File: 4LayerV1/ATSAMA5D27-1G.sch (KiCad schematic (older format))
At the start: 172 parts, among them J1 Conn_01x16, J2 Conn_01x12, J3 USB_B_Micro, J4 Conn_01x02, J5 Conn_01x02, J6 1051620001, J7 USB_A_Micro, Q1 BSS138, Q2 BSS138, Q3 BSS138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

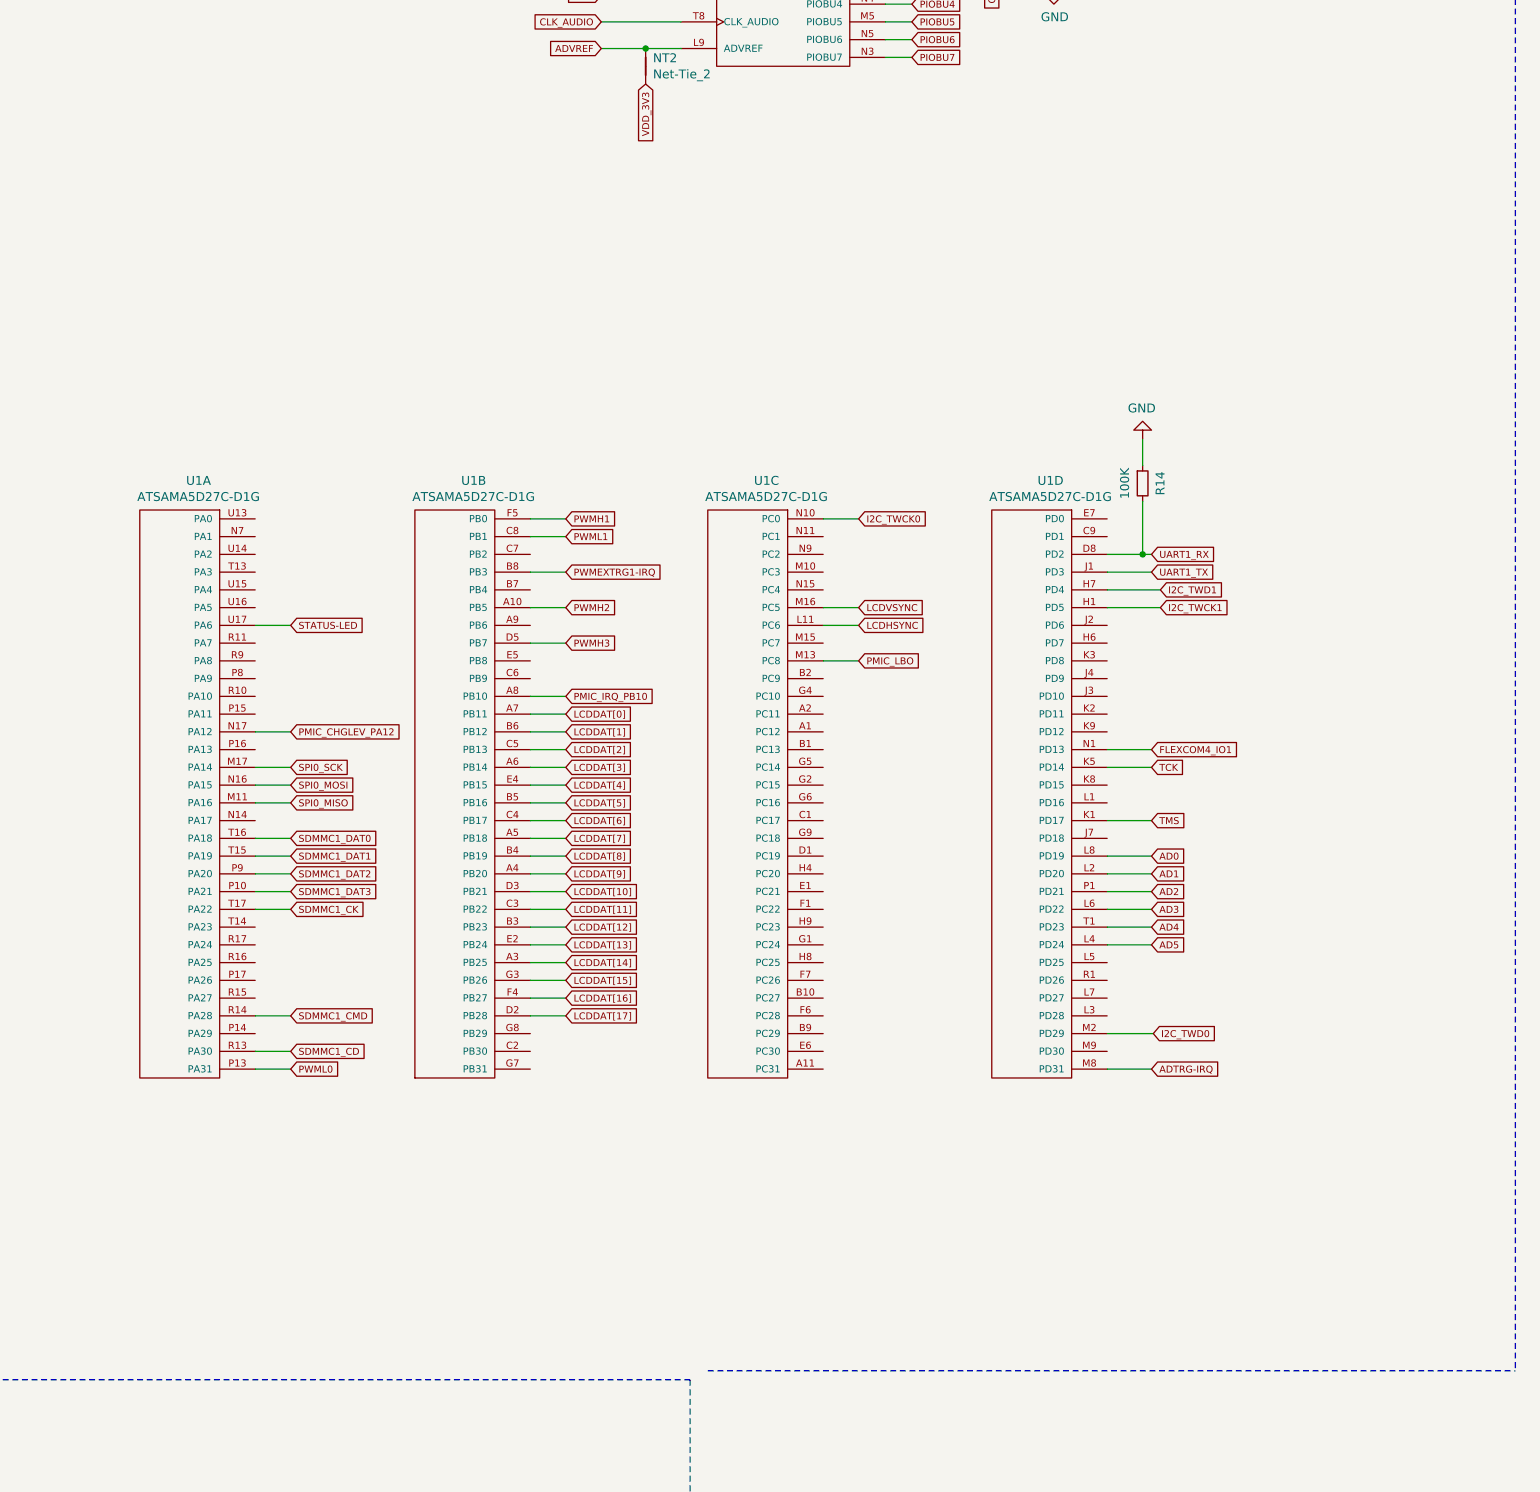
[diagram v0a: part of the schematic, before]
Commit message: Complete 3x 6-bit R2R DACs, with THS7316 buffer.
Using a generic 6-pin connector, as the DE15HD is never going to fit
on the Feather Form factor. I'm not even sure we can get a 6 pin 1mm
pitch header in.
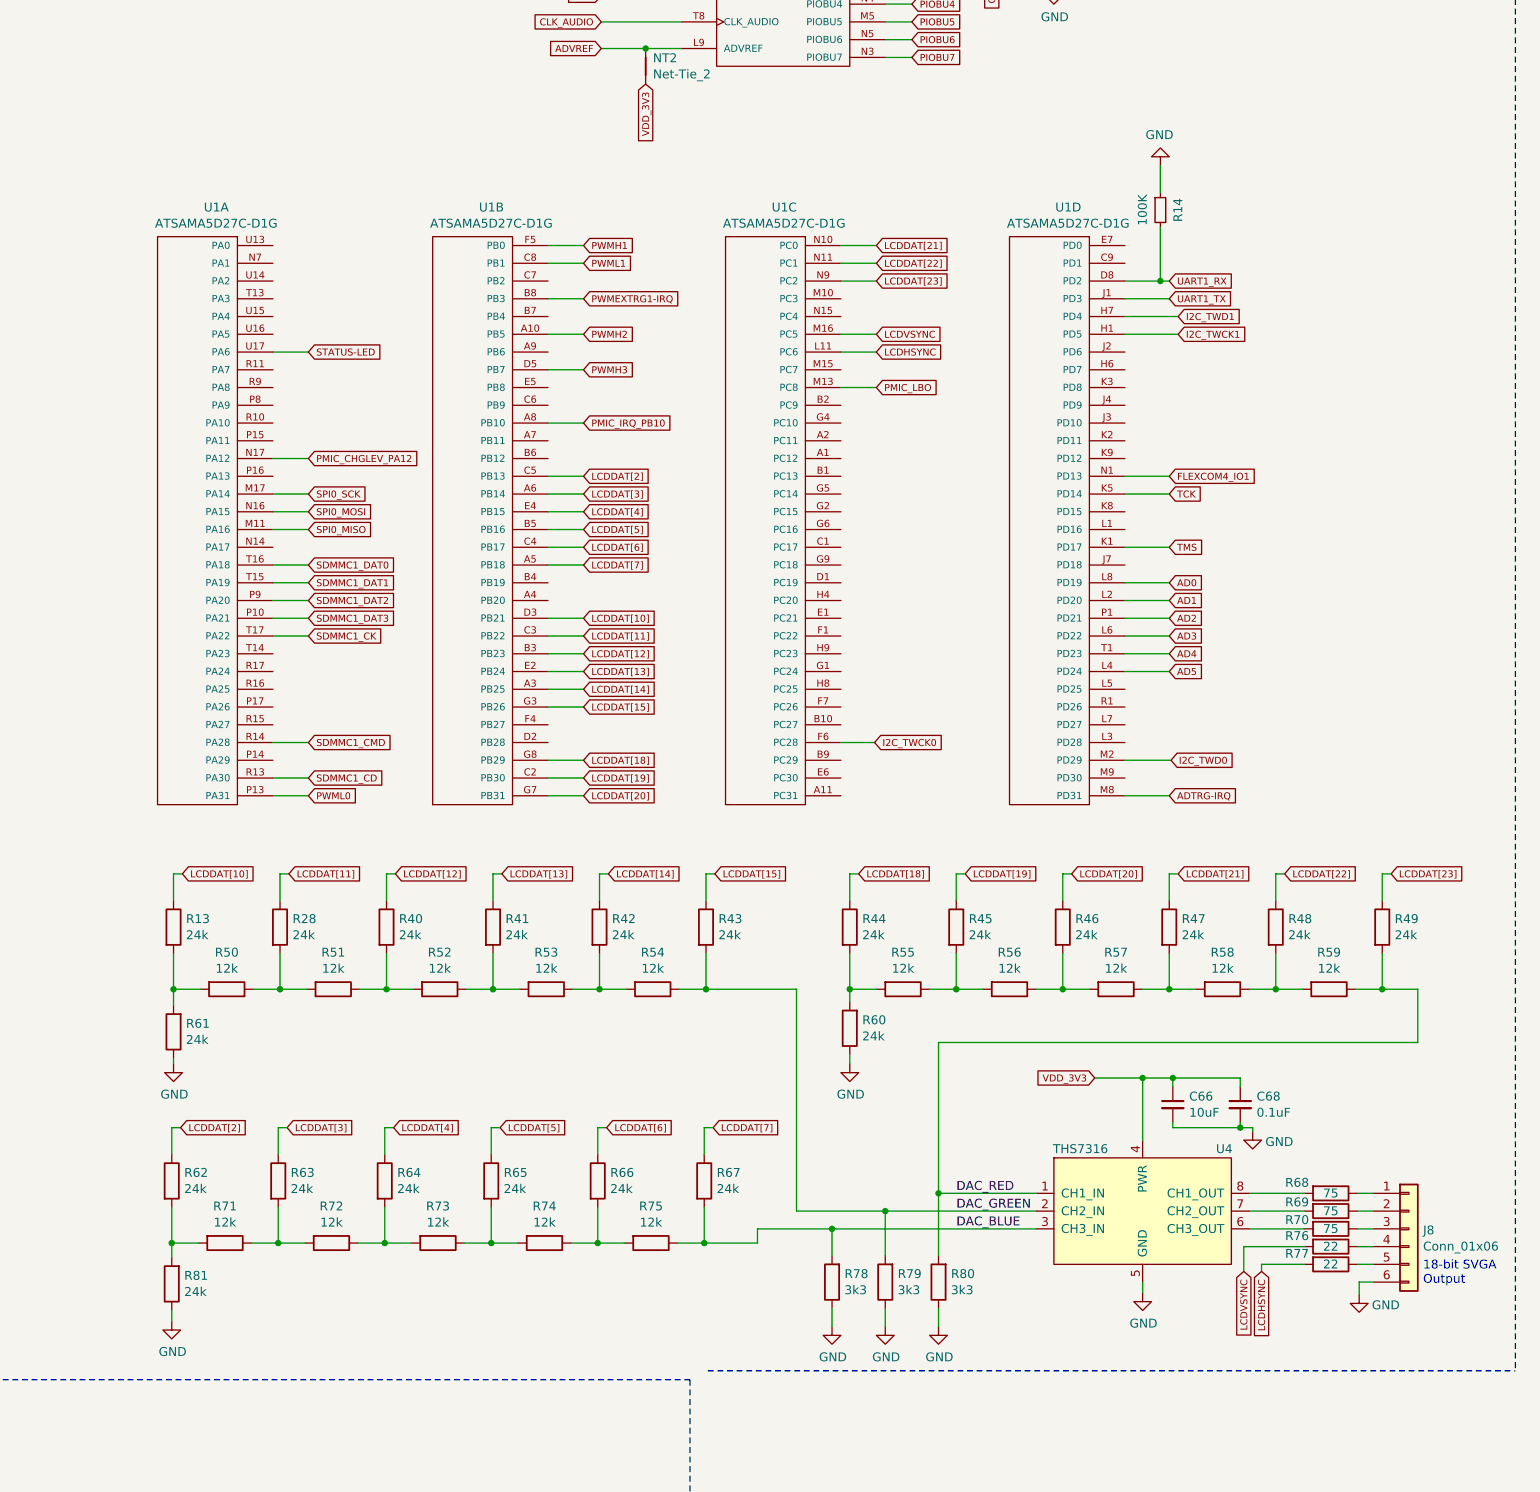
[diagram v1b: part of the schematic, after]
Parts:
- added C66: 10uF, Capacitor_SMD:C_0402_1005Metric, symbol Device:C_Small
- added C68: 0.1uF, Capacitor_SMD:C_0402_1005Metric, symbol Device:C_Small
- added J8: Conn_01x06, symbol Connector_Generic:Conn_01x06
- added R13, R28, R40, R41, R42, R43, R44, R45, R46, R47, R48, R49, R60, R61, R62, R63, R64, R65, R66, R67, R81: 24k, symbol Device:R
- added R50, R51, R52, R53, R54, R55, R56, R57, R58, R59, R71, R72, R73, R74, R75: 12k, symbol Device:R
- added R68, R69, R70: 75, symbol Device:R
- added R76, R77: 22, symbol Device:R
- added R78, R79, R80: 3k3, symbol Device:R
- added U4: THS7316, symbol ATSAMA5D27-1G:THS7316
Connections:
- net GND: now also C66.2, C68.2, J8.6 (Pin_6), R60.1, R61.1, R78.1, R79.1, R80.1, R81.1, U4.5 (GND)
- net I2C_TWCK0: now also U1.F6 (PC28); no longer U1.N10 (PC0)
- net LCDDAT[10]: now also R13.1
- net LCDDAT[11]: now also R28.1
- net LCDDAT[12]: now also R40.1
- net LCDDAT[13]: now also R41.1
- net LCDDAT[14]: now also R42.1
- net LCDDAT[15]: now also R43.1
- net LCDDAT[2]: now also R62.1
- net LCDDAT[3]: now also R63.1
- net LCDDAT[4]: now also R64.1
- net LCDDAT[5]: now also R65.1
- net LCDDAT[6]: now also R66.1
- net LCDDAT[7]: now also R67.1
- net LCDHSYNC: now also R77.2
- net LCDVSYNC: now also R76.2
- net VDD_3V3: now also C66.1, C68.1, U4.4 (PWR)
- net LCDDAT[19]: now reaches U1.C2 (PB30)
- net LCDDAT[19]: now also R45.1
- net LCDDAT[20]: now reaches U1.G7 (PB31)
- net LCDDAT[20]: now also R46.1
- net LCDDAT[18]: now reaches U1.G8 (PB29)
- net LCDDAT[18]: now also R44.1
- net LCDDAT[22]: now reaches U1.N11 (PC1)
- net LCDDAT[22]: now also R48.1
- net LCDDAT[23]: now reaches U1.N9 (PC2)
- net LCDDAT[23]: now also R49.1
- net LCDDAT[0]: no longer names the net of U1.A7 (PB11)
- net LCDDAT[16]: no longer names the net of U1.F4 (PB27)
- net LCDDAT[17]: no longer names the net of U1.D2 (PB28)
- net LCDDAT[1]: no longer names the net of U1.B6 (PB12)
- net LCDDAT[8]: no longer names the net of U1.B4 (PB19)
- net LCDDAT[9]: no longer names the net of U1.A4 (PB20)
- new net: R40.2, R51.1, R52.2
- new net: R41.2, R52.1, R53.2
- new net: R42.2, R53.1, R54.2
- new net: J8.1 (Pin_1), R68.1
- new net: R68.2, U4.8 (CH1_OUT)
- new net: J8.2 (Pin_2), R69.1
- new net: R69.2, U4.7 (CH2_OUT)
- new net: J8.3 (Pin_3), R70.1
- new net: R70.2, U4.6 (CH3_OUT)
- new net: R13.2, R50.2, R61.2
- new net: R28.2, R50.1, R51.2
- new net: J8.4 (Pin_4), R76.1
- new net: J8.5 (Pin_5), R77.1
- new net: R64.2, R72.1, R73.2
- new net: R65.2, R73.1, R74.2
- new net: R66.2, R74.1, R75.2
- new net: R62.2, R71.2, R81.2
- new net: R63.2, R71.1, R72.2
- new net: R46.2, R56.1, R57.2
- new net: R47.2, R57.1, R58.2
- new net: R48.2, R58.1, R59.2
- new net: R44.2, R55.2, R60.2
- new net: R45.2, R55.1, R56.2
- new net DAC_BLUE: R67.2, R75.1, R78.2, U4.3 (CH3_IN)
- new net DAC_GREEN: R43.2, R54.1, R79.2, U4.2 (CH2_IN)
- new net DAC_RED: R49.2, R59.1, R80.2, U4.1 (CH1_IN)
- new net LCDDAT[21]: R47.1, U1.N10 (PC0)
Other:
- note added: "18-bit SVGA\nOutput"
- moved on the sheet: R14, U1A, U1B, U1C, U1D
